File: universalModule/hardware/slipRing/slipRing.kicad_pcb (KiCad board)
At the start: 2 copper layers, 82.8 x 82.8 mm, 10 parts, among them J1 Conn_01x06_Male, J2 Conn_01x06_Male

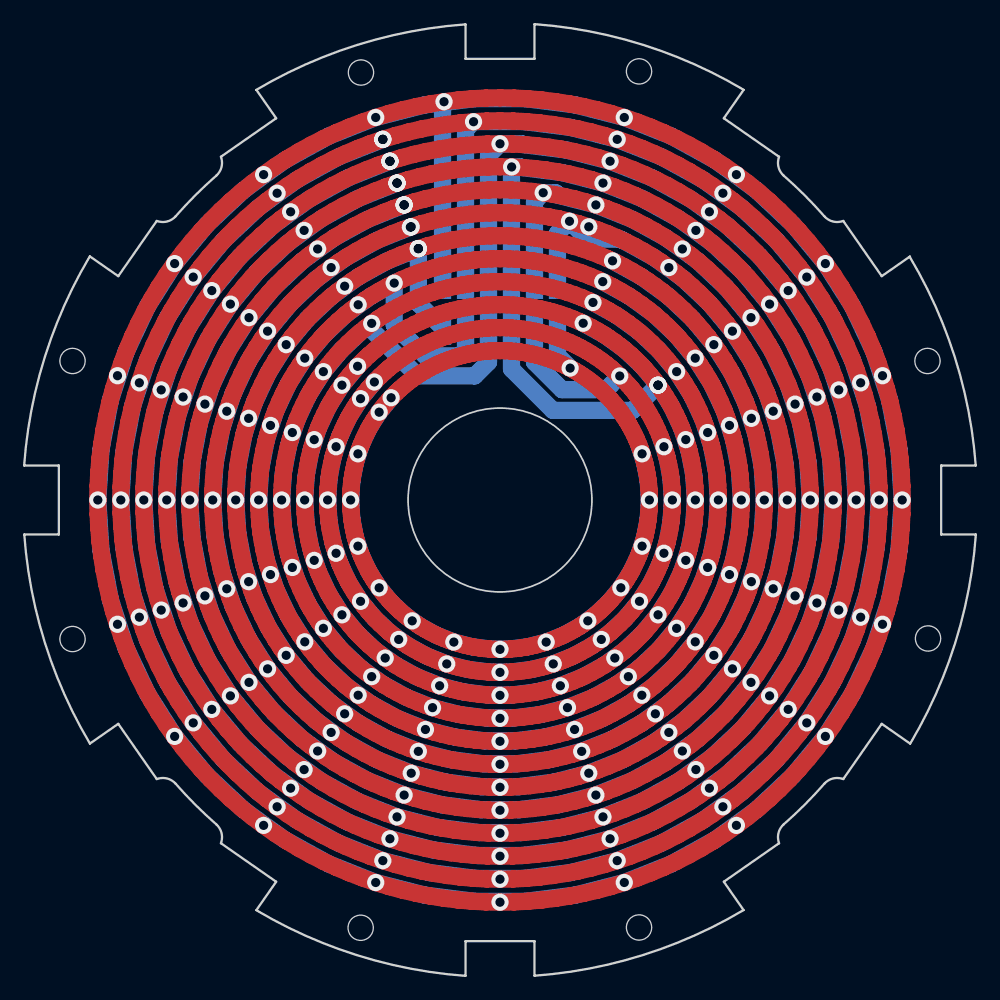
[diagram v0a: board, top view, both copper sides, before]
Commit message: universalModule: Route the control boards
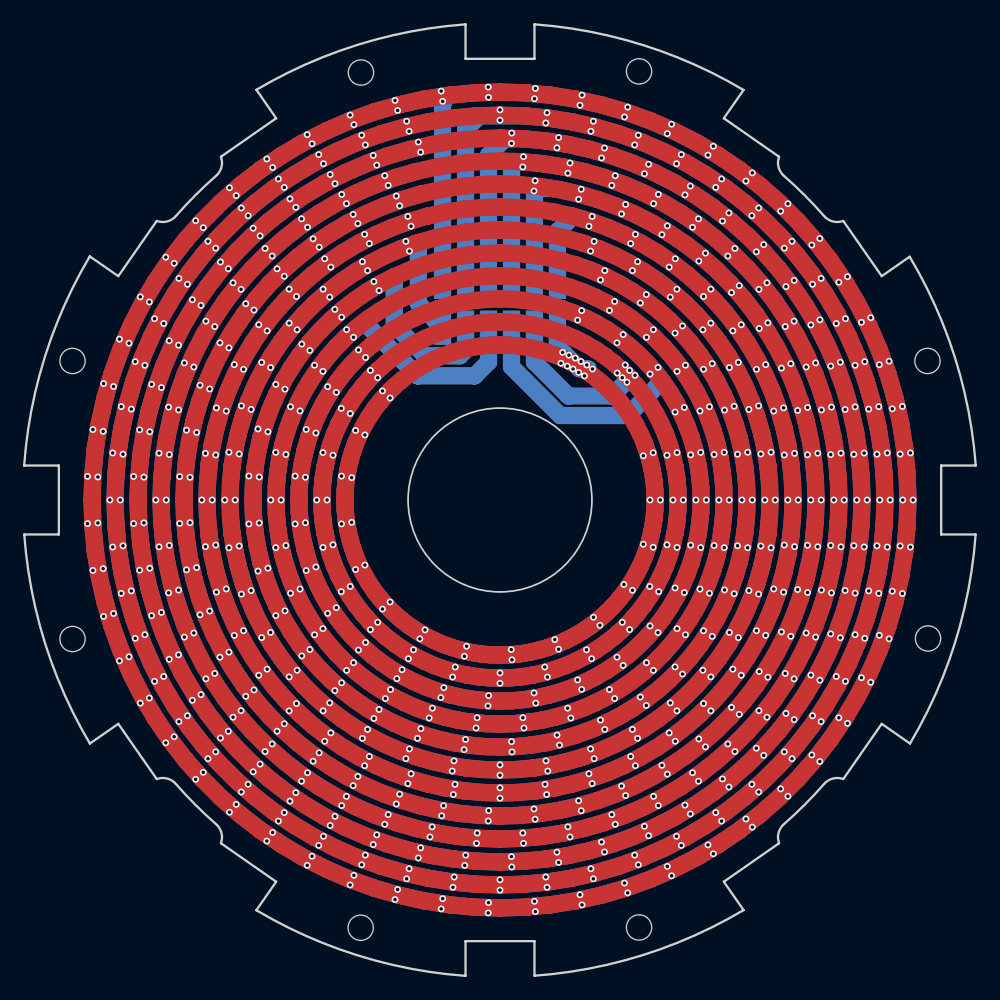
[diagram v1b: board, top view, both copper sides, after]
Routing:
- net /S5: track 335.1 -> 344.9 mm, vias 21 -> 82
- net /S11: track 170.2 -> 179.7 mm, vias 16 -> 40
- net /S2: track 420.5 -> 429.2 mm, vias 21 -> 102
- net /S9: track 233.1 -> 241.8 mm, vias 17 -> 50
- net /S3: track 392.1 -> 400.5 mm, vias 21 -> 96
- net /S4: track 364.2 -> 372.4 mm, vias 21 -> 88
- net /S7: track 279.3 -> 287.3 mm, vias 19 -> 66
- net /S8: track 258.5 -> 266.3 mm, vias 18 -> 58
- net /S12: track 141.2 -> 148.5 mm, vias 16 -> 41
- net /S10: track 211.0 -> 218.0 mm, vias 18 -> 46
- net /S1: track 455.4 -> 461.7 mm, vias 20 -> 110
- net /S6: track 306.2 -> 312.2 mm, vias 21 -> 74
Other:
- board text added: "12"
- board text added: "RoFI UniversalModule: SlipRing v0.2 11/2019"
- board text removed: "8"
- board text removed: "RoFI UniversalModule: SlipRing v0.1 1/2019"
